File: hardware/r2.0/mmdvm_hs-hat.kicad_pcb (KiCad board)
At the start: 4 copper layers, 65.1 x 30.2 mm, 89 parts, among them P1 OLED, P2 Display, P3 SMA, P4 STLINK, P5 USB_C_Plug_USB2.0, U1 ADF7021, U2 STM32F103C8T6, U3 TLV70233_SOT23-5, U4 USBLC6-2, X1 TCXO, Y1 8MHz

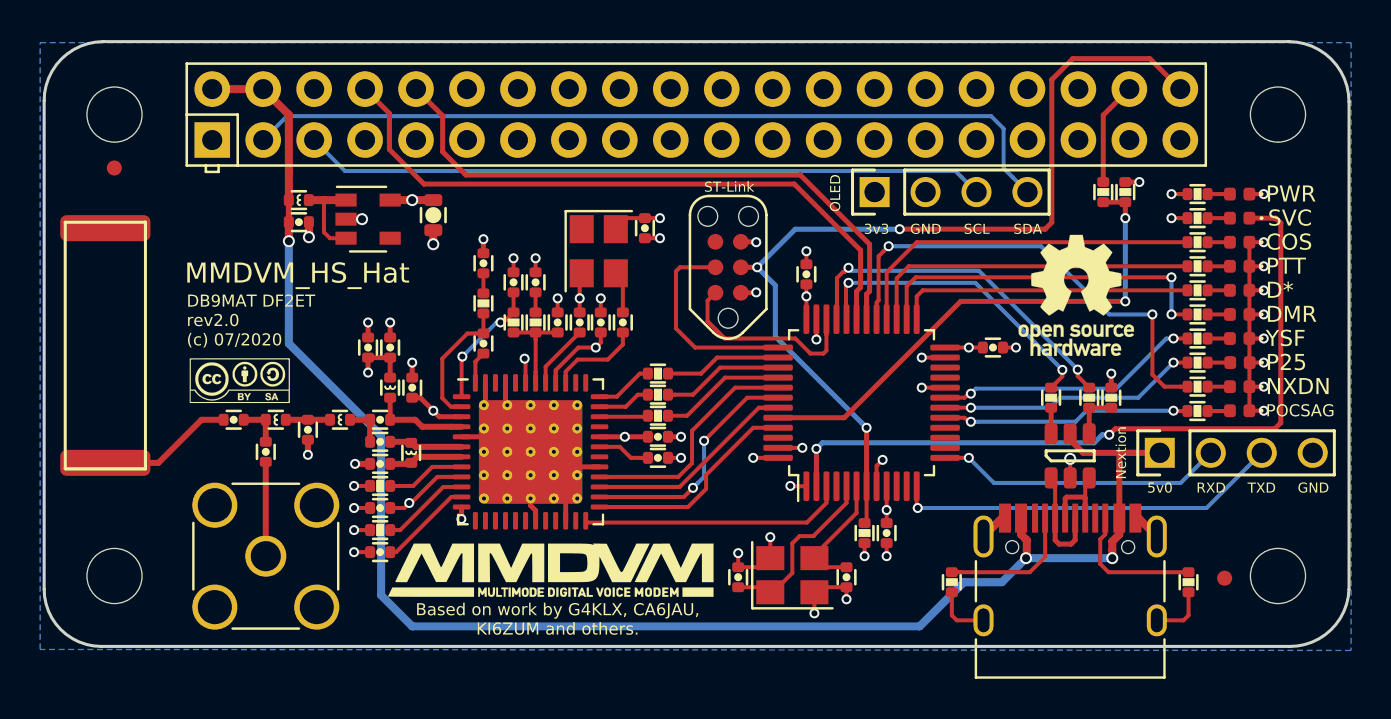
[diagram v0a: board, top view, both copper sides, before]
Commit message: Small silk screen changes
Final Revision 2.0, tested and working
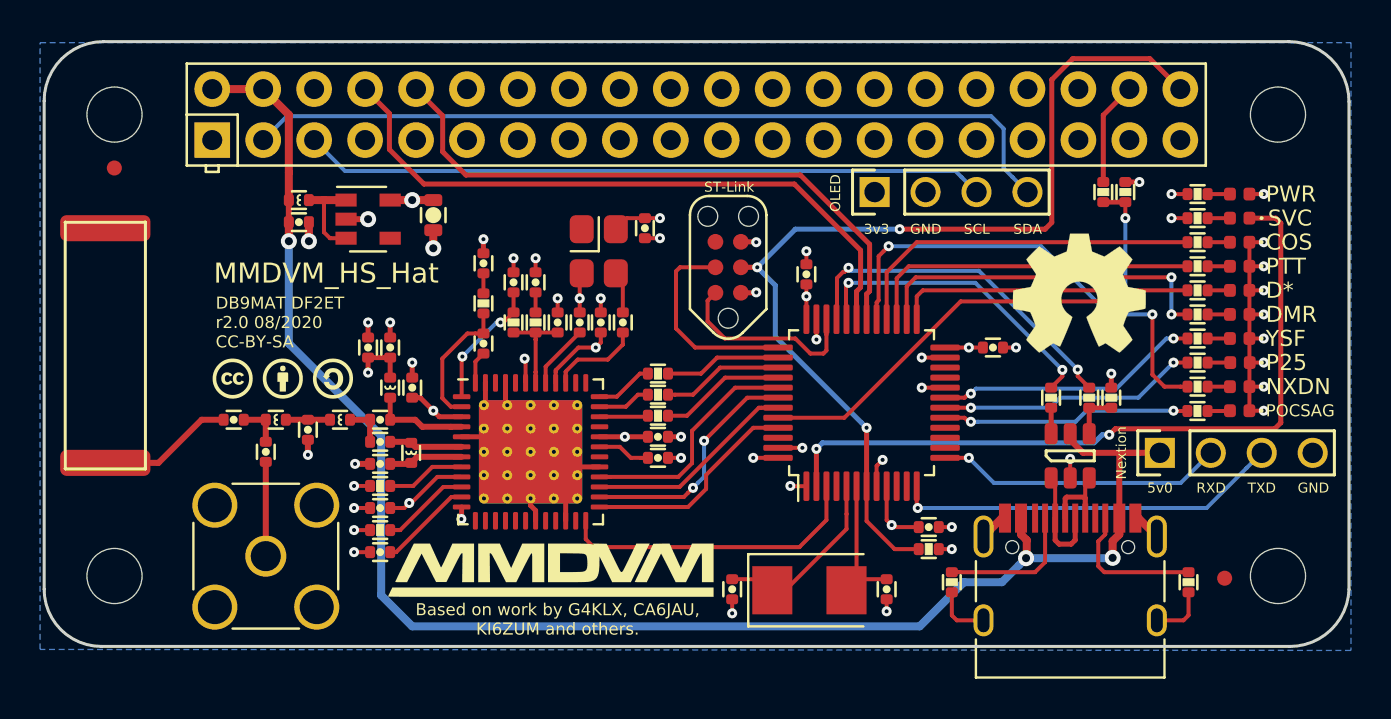
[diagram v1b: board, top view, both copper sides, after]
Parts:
- removed the G*** at (165.2, 122.5)
- removed the REF** at (206.9, 118.2)
- added REF**: OSHW-Symbol_6.7x6mm_SilkScreen, Symbol:OSHW-Symbol_6.7x6mm_SilkScreen, F.Cu at (207.1, 118.2)
- added REF**: Symbol_CC-SA_SilkScreen_2mm, pkl_logos:Symbol_CC-SA_SilkScreen_2mm, F.Cu at (169.8, 122.4)
- added REF**: Symbol_CC-BY_SilkScreen_2mm, pkl_logos:Symbol_CC-BY_SilkScreen_2mm, F.Cu at (167.3, 122.4)
- added REF**: Symbol_CC_SilkScreen_2mm, pkl_logos:Symbol_CC_SilkScreen_2mm, F.Cu at (164.8, 122.4)
- Y1: footprint Crystal:Crystal_SMD_3225-4Pin_3.2x2.5mm -> Crystal:Crystal_SMD_5032-2Pin_5.0x3.2mm
- moved R7 3.30 mm to (199.6, 130.9), turned to 0 degrees
- moved C24 2.12 mm to (199.6, 129.8), turned to 0 degrees
- moved C23 2.09 mm to (197.4, 132.9)
- moved Y1 1.13 mm to (193.6, 132.9)
- moved C21 0.67 mm to (189.8, 132.9), turned to 90 degrees
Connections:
- Y1 pad 2: GND -> Net-(C23-Pad2)
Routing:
- net GND: track 78.7 -> 73.8 mm, vias 46 -> 44
- net NRST: track 46.1 -> 49.1 mm
- net CE: track 13.3 -> 15.3 mm
- net VDD: track 33.3 -> 34.9 mm
- net Net-(C23-Pad2): track 6.24 -> 7.62 mm
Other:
- rule via_min_drill: 0.3 -> 0.2
- board text added: "DB9MAT DF2ET r2.0 08/2020 CC-BY-SA"
- board text removed: "DB9MAT DF2ET rev2.0 (c) 07/2020"
